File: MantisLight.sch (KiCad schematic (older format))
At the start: 29 parts, among them IC1 ATMEGA32-A, K1 SPI, K3 Vin12V, P1 IMP, P2 PB2, P3 PC7, P4 PC6, P5 PORTA, P6 JTAG, P8 AREF, P9 BUTTON, U2 TSL2561, U5 7805, X1 16 MHz

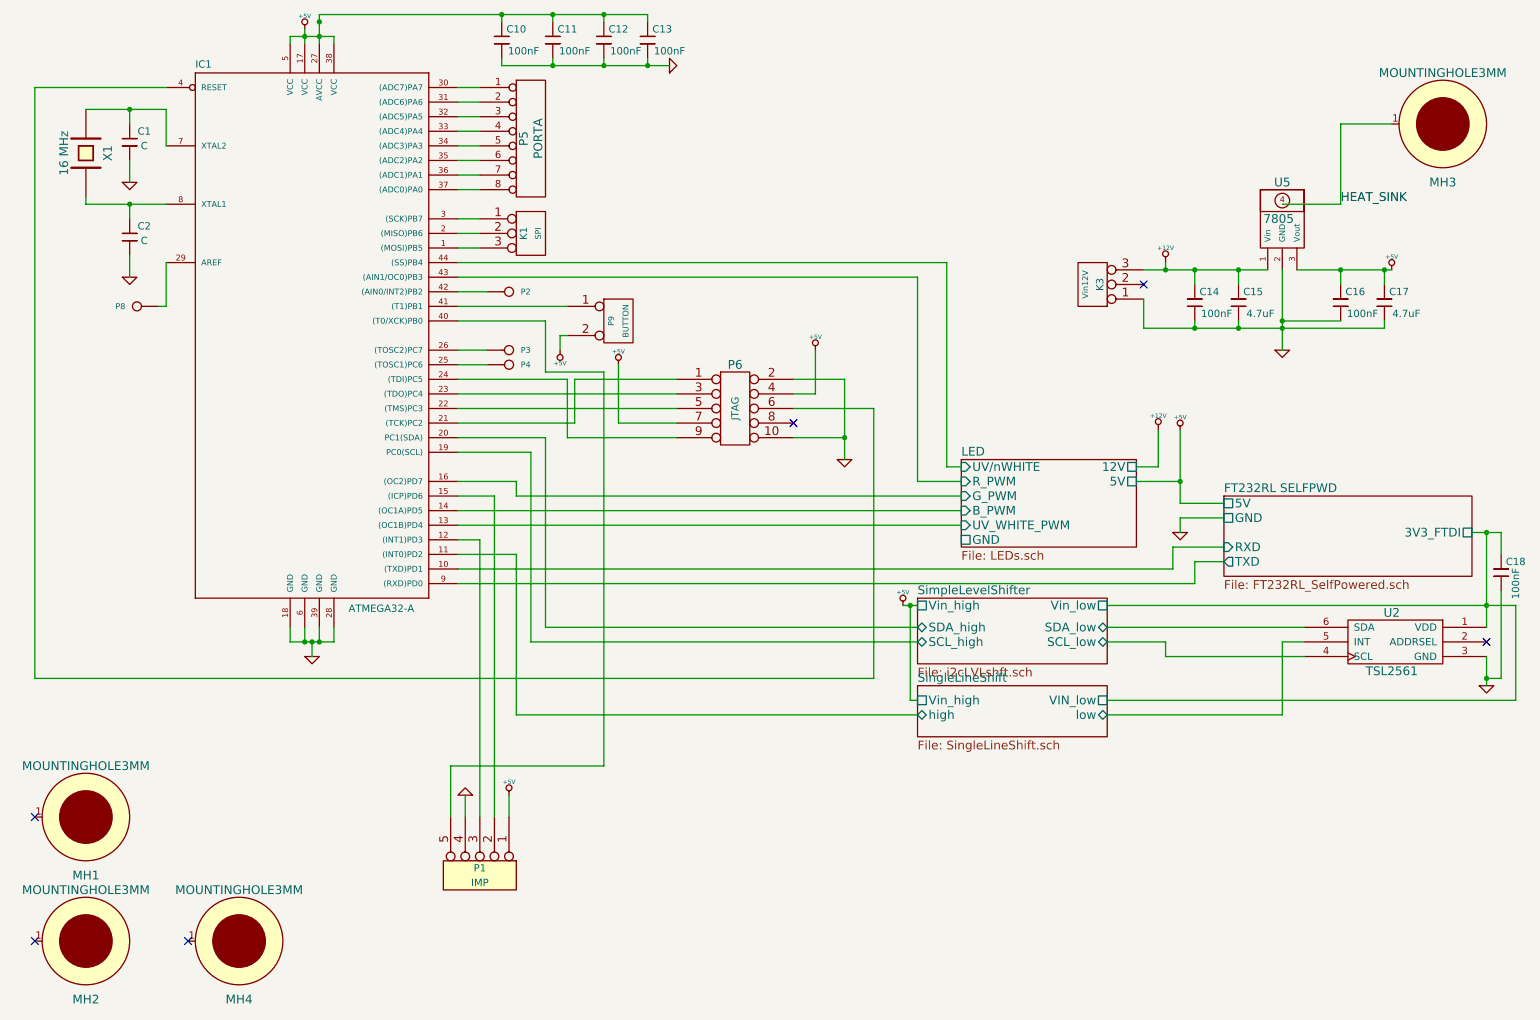
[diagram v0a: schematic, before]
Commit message: 
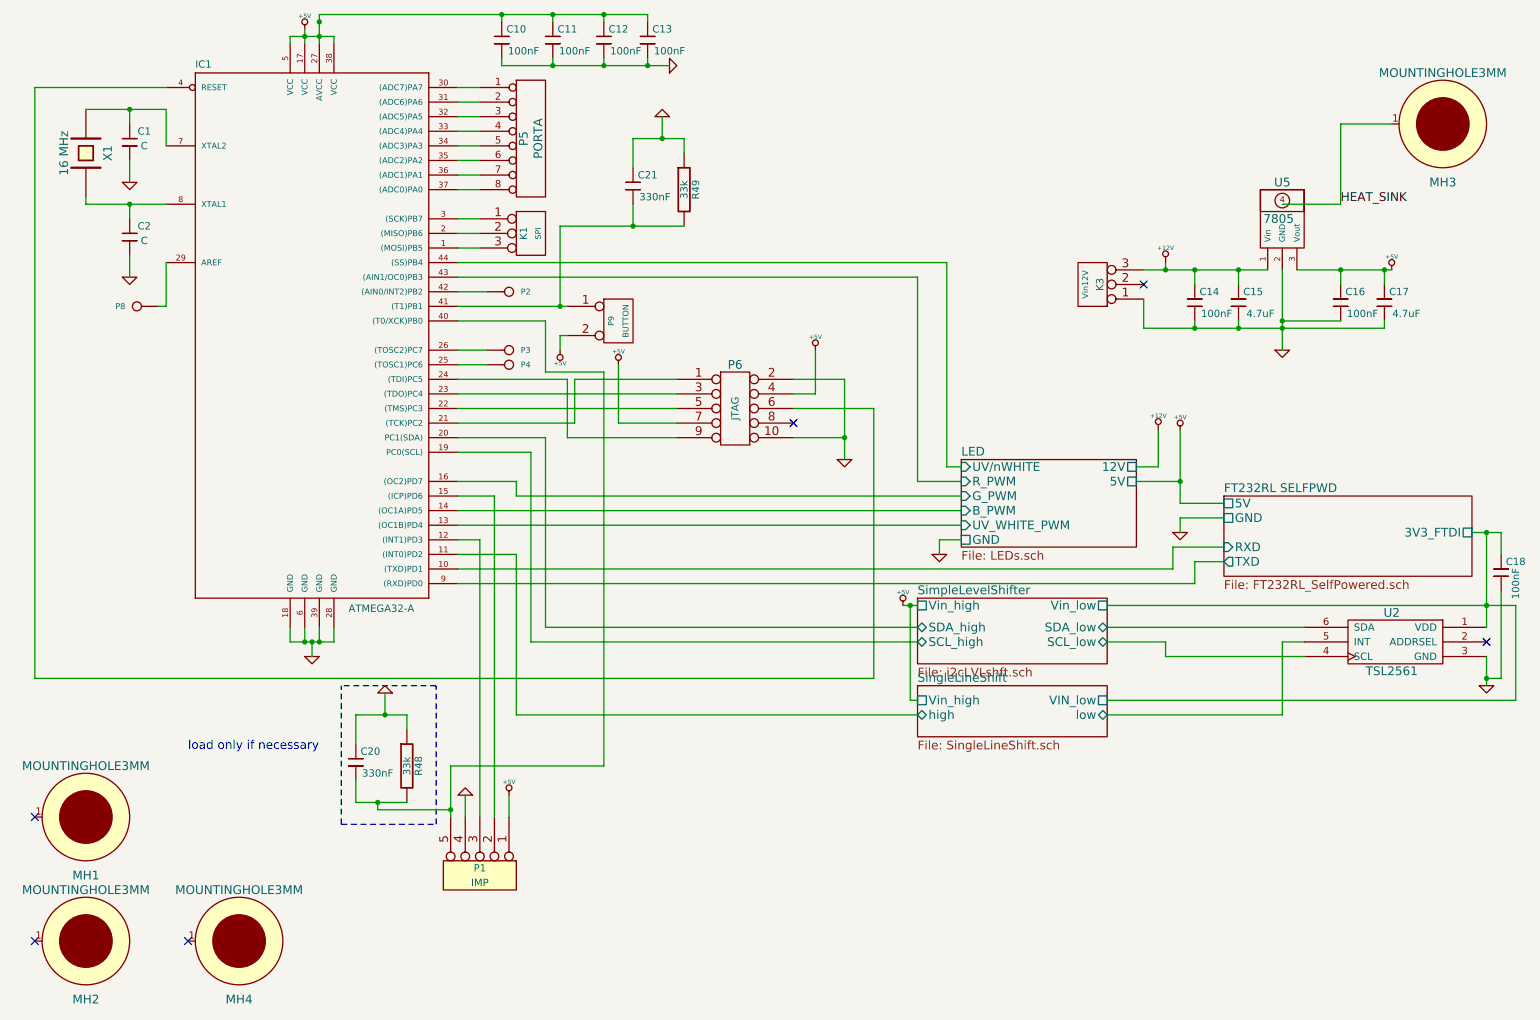
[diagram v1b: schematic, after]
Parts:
- added C20, C21: 330nF, symbol C
- added R48, R49: 33k, symbol R
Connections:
- net GND: now also C20.1, C21.1, R48.1, R49.1
- net at IC1.40 ((T0/XCK)PB0), P1.5: now also C20.2, R48.2
- net at IC1.41 ((T1)PB1), P9.1 (P1): now also C21.2, R49.2
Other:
- note added: "load only if necessary"
